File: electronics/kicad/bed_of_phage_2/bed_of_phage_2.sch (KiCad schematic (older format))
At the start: 12 parts, among them J1 CONN_03, J2 CONN_03, P1 CONN_8, U1 LM358N

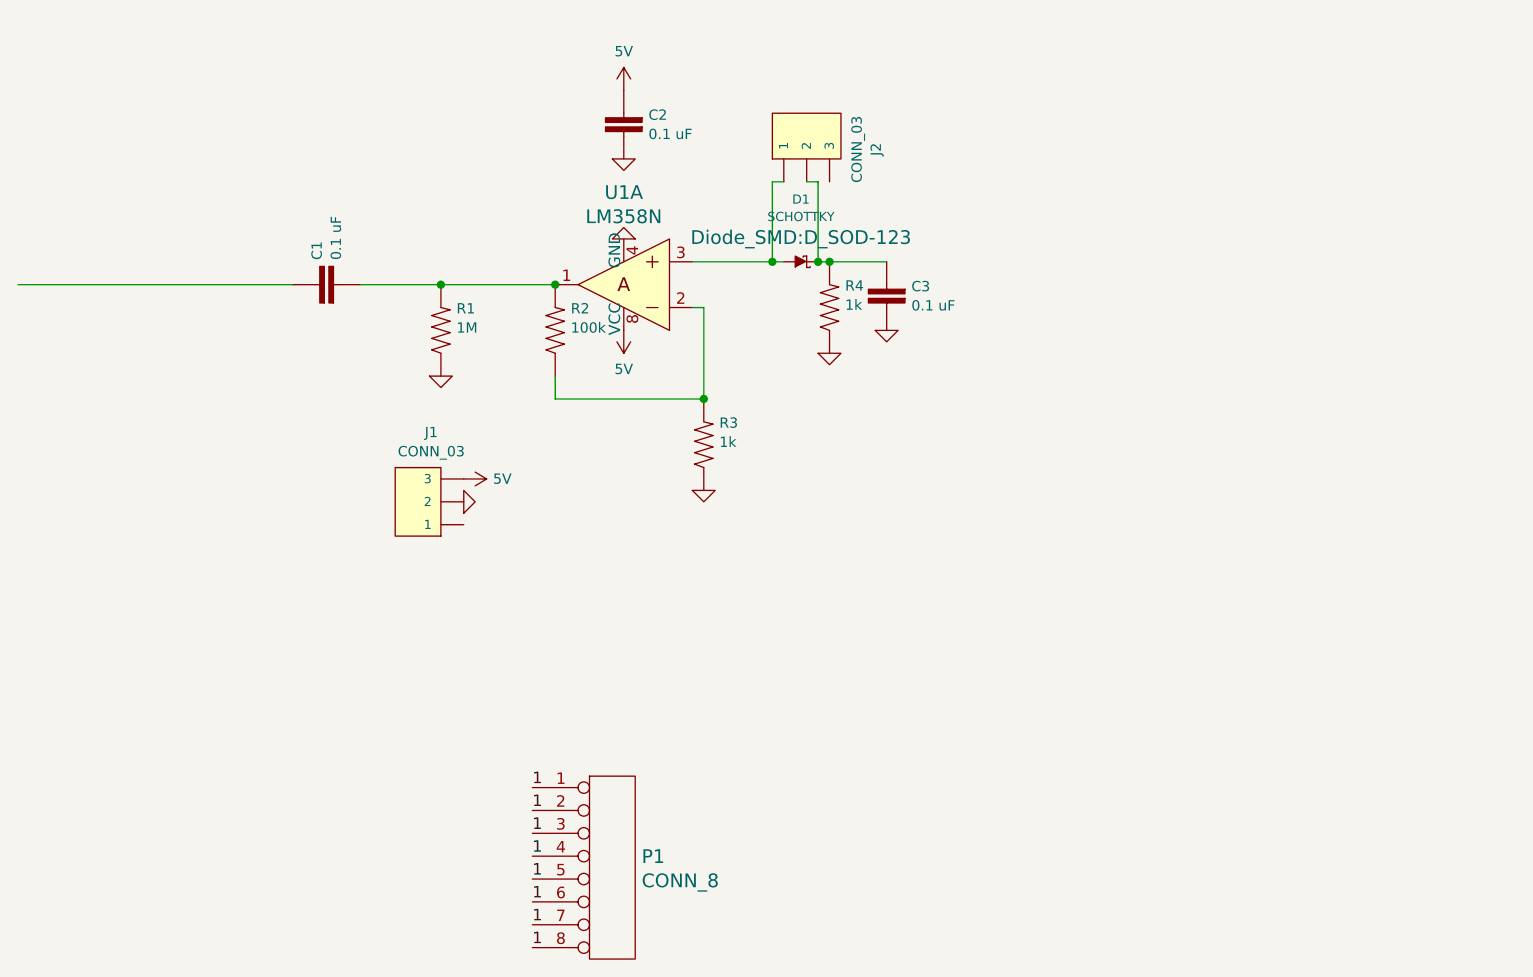
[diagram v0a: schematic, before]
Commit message: Screwed up a simple op-amp circuit
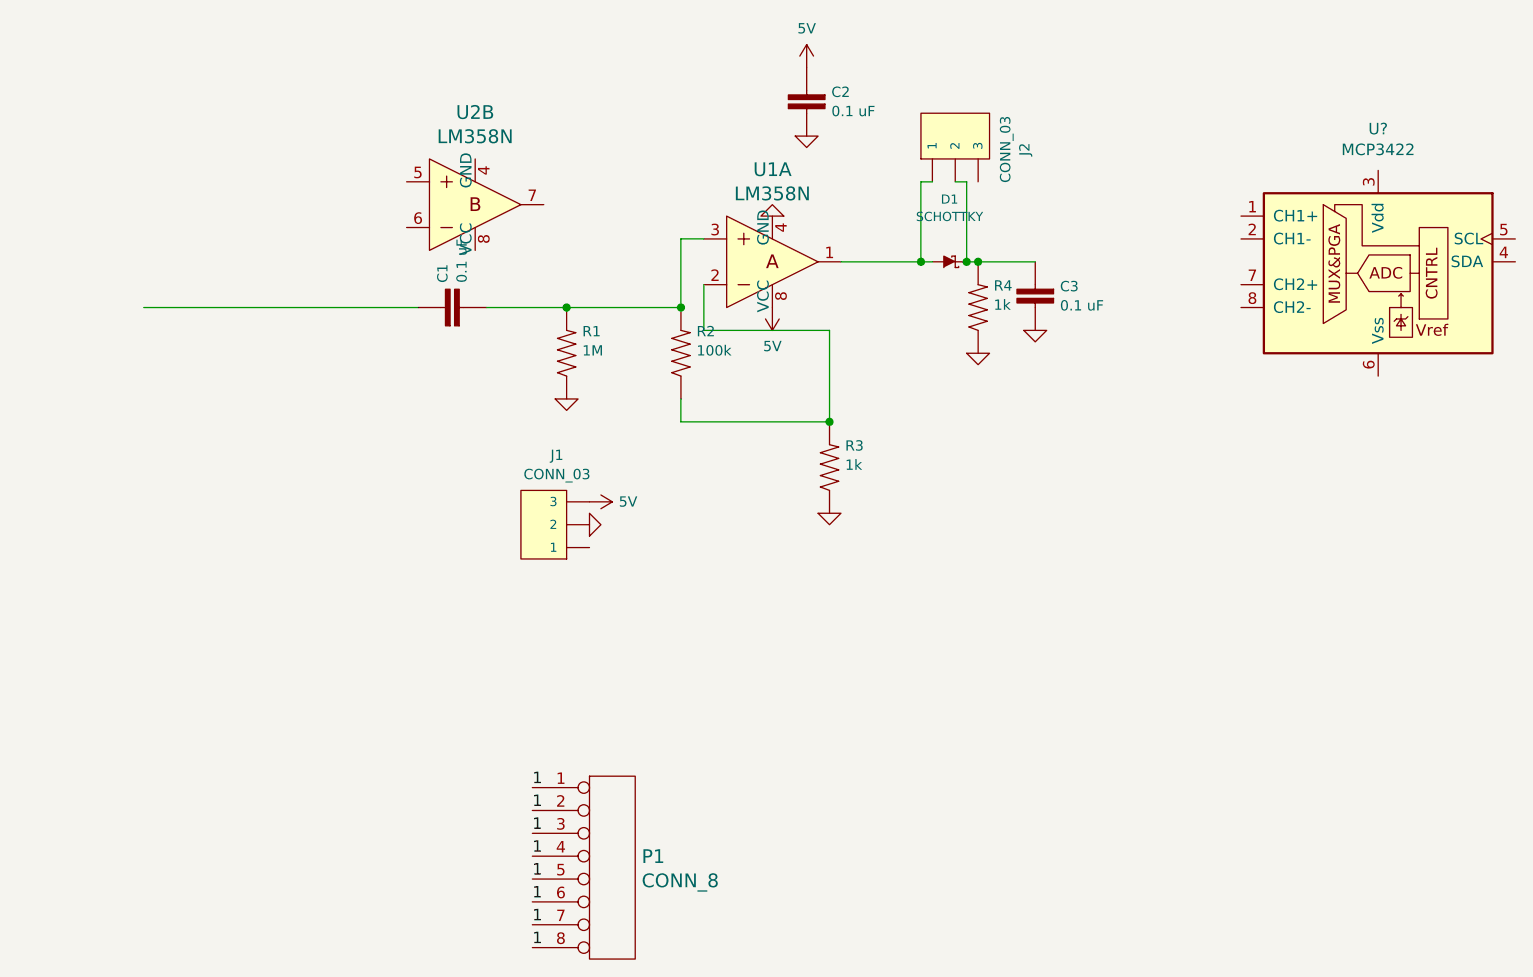
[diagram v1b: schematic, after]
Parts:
- added U2: LM358N, digikey-footprints:DIP-8_W7.62mm, symbol dk_Linear-Amplifiers-Instrumentation-OP-Amps-Buffer-Amps:LM358N
- added U?: MCP3422, symbol Analog_ADC:MCP3422
- D1: footprint Diode_SMD:D_SOD-123 -> (none)
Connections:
- wire segments 15 -> 18
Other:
- moved on the sheet: C1, C2, C3, D1, J1, J2, R1, R2, R3, R4, U1A

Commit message: nope, I didn't screw that up.
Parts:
- removed U2: LM358N, digikey-footprints:DIP-8_W7.62mm, symbol dk_Linear-Amplifiers-Instrumentation-OP-Amps-Buffer-Amps:LM358N
- removed U?: MCP3422, symbol Analog_ADC:MCP3422
- D1: footprint (none) -> Diode_SMD:D_SOD-123
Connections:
- wire segments 18 -> 15
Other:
- moved on the sheet: C1, C2, C3, D1, J1, J2, R1, R2, R3, R4, U1A

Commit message: test 1
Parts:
- D1: footprint Diode_SMD:D_SOD-123 -> (none)
- R1: value 1M -> 110k
- R2: value 100k -> 110k
- U1: value LM358N -> TLV9062IDR
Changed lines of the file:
@@
 Comment4 ""
 $EndDescr
-$Comp
-L conn:CONN_8 P1
-U 1 1 60D91A6E
-P 3300 5300
-F 0 "P1" H 3428 5348 60  0000 L CNN
-F 1 "CONN_8" H 3428 5242 60  0000 L CNN
-F 2 "Connectors2:1X08_SMD_MALE" H 3300 5300 50  0001 C CNN
-F 3 "" H 3300 5300 50  0001 C CNN
-	1    3300 5300
-	1    0    0    -1
-$EndComp
 Text Label 2950 4950 0    50   ~ 0
 1
@@
 F 0 "D1" H 4125 2923 40  0000 C CNN
 F 1 "SCHOTTKY" H 4125 2847 40  0000 C CNN
-F 2 "Diode_SMD:D_SOD-123" H 4125 2756 60  0000 C CNN
+F 2 "" H 4125 2756 60  0000 C CNN
 F 3 "" H 4100 2650 60  0000 C CNN
 	1    4100 2650
@@
 P 3050 2950
 F 0 "R2" V 3145 2882 45  0000 R CNN
-F 1 "100k" V 3061 2882 45  0000 R CNN
+F 1 "110k" V 3061 2882 45  0000 R CNN
 F 2 "0603" H 3050 3100 20  0001 C CNN
 F 3 "" H 3050 2950 60  0001 C CNN
@@
 P 2550 2950
 F 0 "R1" V 2645 2882 45  0000 R CNN
-F 1 "1M" V 2561 2882 45  0000 R CNN
+F 1 "110k" V 2561 2882 45  0000 R CNN
 F 2 "0603" H 2550 3100 20  0001 C CNN
 F 3 "" H 2550 2950 60  0001 C CNN
@@
 P 3350 2750
 F 0 "U1" H 3350 2347 60  0000 C CNN
-F 1 "LM358N" H 3350 2453 60  0000 C CNN
+F 1 "TLV9062IDR" H 3350 2453 60  0000 C CNN
 F 2 "Package_SO:SOIC-8_3.9x4.9mm_P1.27mm" H 3550 2950 60  0001 L CNN
 F 3 "https://www.fairchildsemi.com/datasheets/LM/LM258A.pdf" H 3550 3050 60  0001 L CNN
@@
 	-1   0    0    1
 $EndComp
+$Comp
+L conn:CONN_8 P1
+U 1 1 60D91A6E
+P 3300 5300
+F 0 "P1" H 3428 5348 60  0000 L CNN
+F 1 "CONN_8" H 3428 5242 60  0000 L CNN
+F 2 "Connectors2:1X08_SMD_MALE" H 3300 5300 50  0001 C CNN
+F 3 "" H 3300 5300 50  0001 C CNN
+	1    3300 5300
+	1    0    0    -1
+$EndComp
 $EndSCHEMATC
